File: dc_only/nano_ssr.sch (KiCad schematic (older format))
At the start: 35 parts, among them K1 CONN_3, K2 CONN_3, P1 CONN_5, P10 2X_BLOCK_CONN, P11 2X_BLOCK_CONN, P12 2X_BLOCK_CONN, P2 CONN_5X2, P3 CONN_4, P4 CONN_2, P5 2X_BLOCK_CONN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

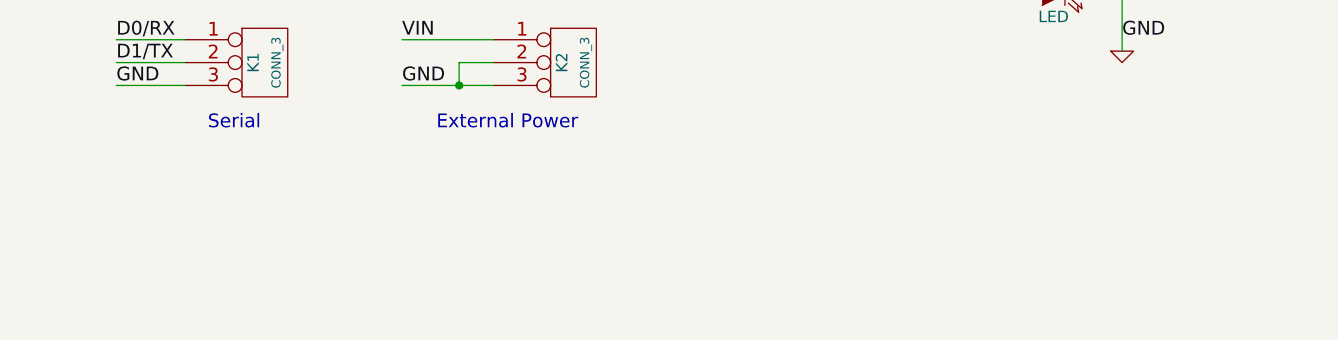
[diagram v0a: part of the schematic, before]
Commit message: Added link to Arduino and Python libraries on schematic.
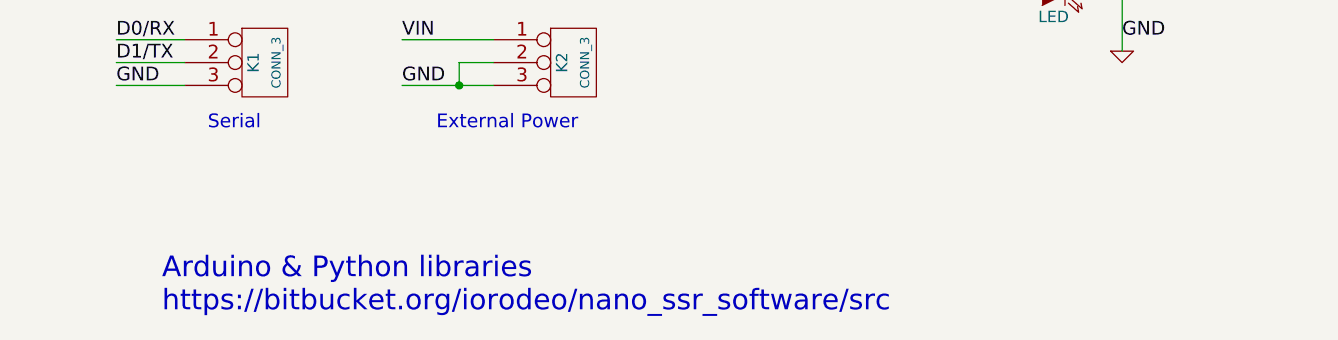
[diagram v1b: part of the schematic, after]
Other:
- note added: "Arduino & Python libraries \nhttps://bitbucket.org/iorodeo/nano_ssr_software/src"
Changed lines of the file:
@@
 Sheet 1 1
 Title ""
-Date "4 jun 2012"
+Date "19 mar 2018"
 Rev ""
 Comp ""
@@
 	1    0    0    -1
 $EndComp
+Text Notes 2350 7100 0    90   ~ 0
+Arduino & Python libraries \nhttps://bitbucket.org/iorodeo/nano_ssr_software/src
 $EndSCHEMATC
